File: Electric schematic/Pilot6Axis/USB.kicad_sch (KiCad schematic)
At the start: 20 parts, among them J2 USB_C_Receptacle_USB2.0_16P, Q1 S9014, Q3 S9014, U2 USBLC6-2SC6, U3 CP2102N-Axx-xQFN28

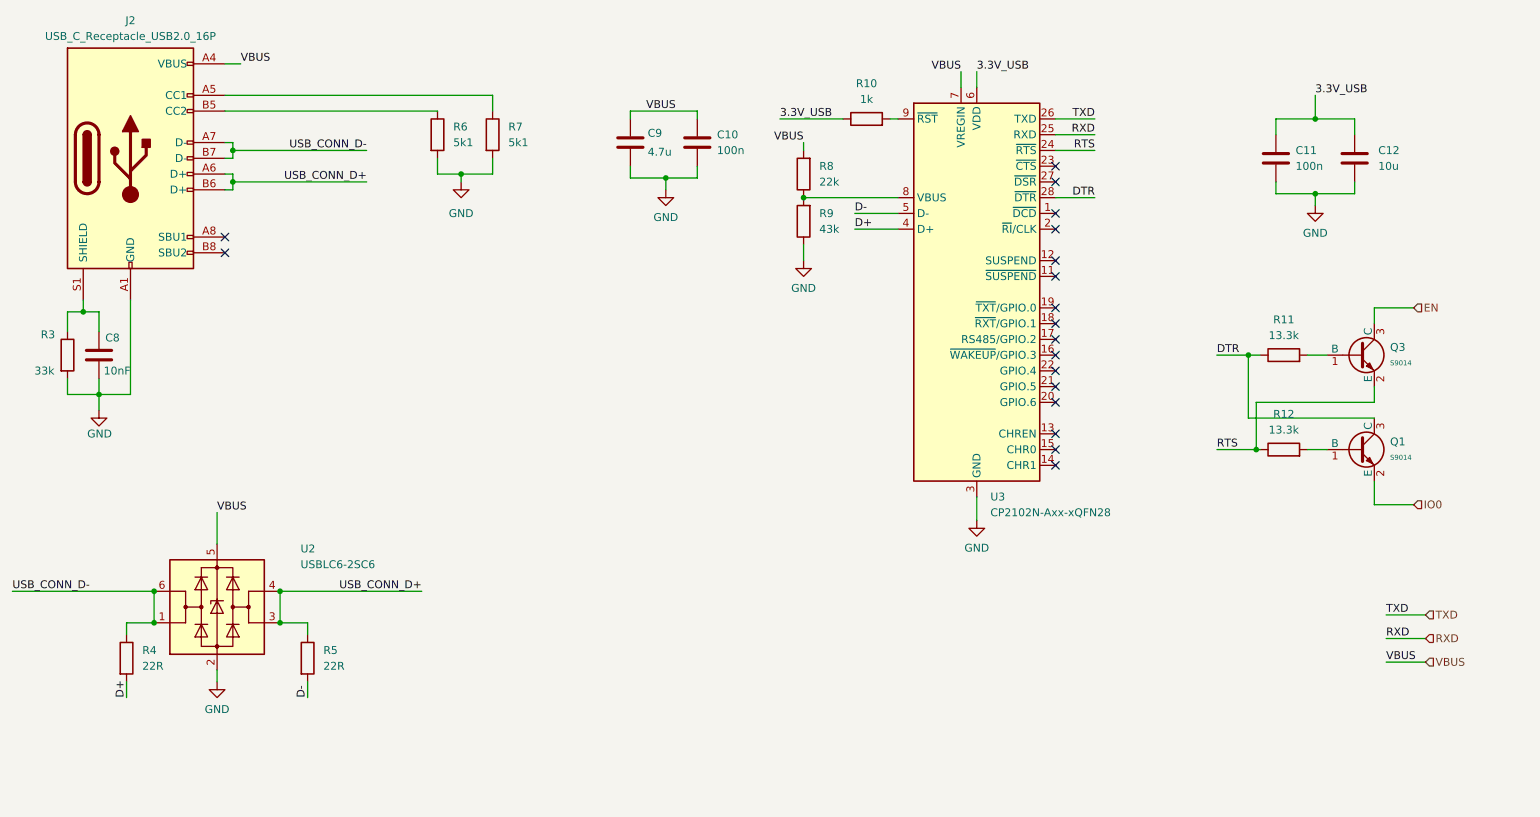
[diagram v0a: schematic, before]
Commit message: update schematic to kicajd 9.0,    fixed usb D=/D- wrongly inerconnected , otherwise pcb seems to be woekring
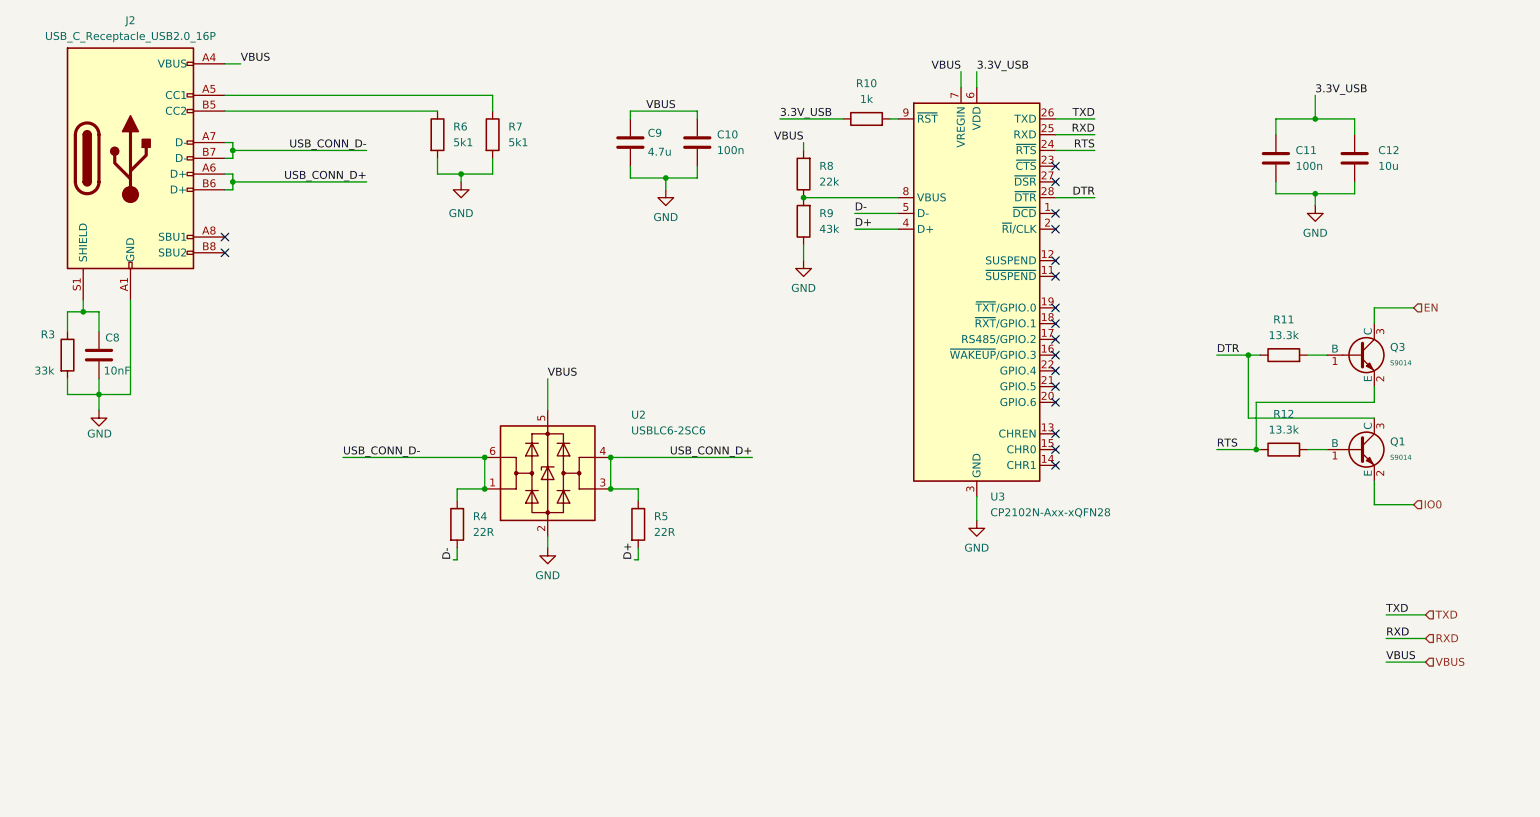
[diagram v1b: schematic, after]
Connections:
- net D+: now also R5.2; no longer R4.2
- net D-: now also R4.2; no longer R5.2
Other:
- moved on the sheet: R4, R5, U2
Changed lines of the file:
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@@
 (kicad_sch
-	(version 20231120)
+	(version 20250114)
 	(generator "eeschema")
-	(generator_version "8.0")
+	(generator_version "9.0")
 	(paper "A4")
 	(junction
@@
 	)
 	(junction
-		(at 50.8 116.84)
+		(at 104.14 95.25)
 		(diameter 0)
 		(color 0 0 0 0)
@@
 	)
 	(junction
-		(at 50.8 121.92)
+		(at 104.14 100.33)
 		(diameter 0)
 		(color 0 0 0 0)
@@
 	)
 	(junction
-		(at 71.12 116.84)
+		(at 124.46 95.25)
 		(diameter 0)
 		(color 0 0 0 0)
@@
 	)
 	(junction
-		(at 71.12 121.92)
+		(at 124.46 100.33)
 		(diameter 0)
 		(color 0 0 0 0)
@@
 	(wire
 		(pts
-			(xy 71.12 121.92) (xy 75.565 121.92)
+			(xy 124.46 100.33) (xy 128.905 100.33)
 		)
 		(stroke
@@
 	(wire
 		(pts
+			(xy 99.695 111.76) (xy 99.695 109.855)
+		)
+		(stroke
+			(width 0)
+			(type default)
+		)
+	)
+	(wire
+		(pts
 			(xy 85.09 45.72) (xy 63.5 45.72)
 		)
@@
 	(wire
 		(pts
-			(xy 46.355 121.92) (xy 46.355 123.825)
+			(xy 99.695 100.33) (xy 99.695 102.235)
 		)
 		(stroke
@@
 	(wire
 		(pts
-			(xy 71.12 116.84) (xy 93.98 116.84)
+			(xy 124.46 95.25) (xy 147.32 95.25)
 		)
 		(stroke
@@
 	(wire
 		(pts
-			(xy 27.94 116.84) (xy 50.8 116.84)
+			(xy 81.28 95.25) (xy 104.14 95.25)
 		)
 		(stroke
@@
 	(wire
 		(pts
+			(xy 128.27 111.76) (xy 128.905 111.76)
+		)
+		(stroke
+			(width 0)
+			(type default)
+		)
+	)
+	(wire
+		(pts
 			(xy 36.83 82.55) (xy 36.83 85.09)
 		)
@@
 	(wire
 		(pts
-			(xy 60.96 104.14) (xy 60.96 109.22)
+			(xy 114.3 82.55) (xy 114.3 87.63)
 		)
 		(stroke
@@
 	(wire
 		(pts
-			(xy 60.96 129.54) (xy 60.96 131.445)
+			(xy 114.3 107.95) (xy 114.3 109.855)
 		)
 		(stroke
@@
 	(wire
 		(pts
-			(xy 62.23 44.45) (xy 63.5 44.45)
+			(xy 128.905 111.76) (xy 128.905 109.855)
 		)
 		(stroke
@@
 	(wire
 		(pts
-			(xy 236.855 78.74) (xy 240.03 78.74)
+			(xy 62.23 44.45) (xy 63.5 44.45)
 		)
 		(stroke
@@
 	(wire
 		(pts
-			(xy 100.33 49.53) (xy 100.33 50.8)
+			(xy 236.855 78.74) (xy 240.03 78.74)
 		)
 		(stroke
@@
 	(wire
 		(pts
-			(xy 238.125 52.705) (xy 238.125 54.61)
+			(xy 100.33 49.53) (xy 100.33 50.8)
 		)
 		(stroke
@@
 	(wire
 		(pts
-			(xy 228.6 93.98) (xy 229.235 93.98)
+			(xy 238.125 52.705) (xy 238.125 54.61)
 		)
 		(stroke
@@
 	(wire
 		(pts
-			(xy 41.91 71.755) (xy 39.37 71.755)
+			(xy 228.6 93.98) (xy 229.235 93.98)
 		)
 		(stroke
@@
 	(wire
 		(pts
-			(xy 238.125 52.705) (xy 244.475 52.705)
+			(xy 41.91 71.755) (xy 39.37 71.755)
 		)
 		(stroke
@@
 	(wire
 		(pts
-			(xy 50.8 116.84) (xy 50.8 121.92)
+			(xy 238.125 52.705) (xy 244.475 52.705)
 		)
 		(stroke
@@
 	(wire
 		(pts
-			(xy 247.65 102.87) (xy 254 102.87)
+			(xy 104.14 95.25) (xy 104.14 100.33)
 		)
 		(stroke
@@
 	(wire
 		(pts
-			(xy 46.355 131.445) (xy 46.355 133.985)
+			(xy 247.65 102.87) (xy 254 102.87)
 		)
 		(stroke
@@
 	(wire
 		(pts
-			(xy 50.8 121.92) (xy 46.355 121.92)
+			(xy 104.14 100.33) (xy 99.695 100.33)
 		)
 		(stroke
@@
 	(wire
 		(pts
-			(xy 75.565 121.92) (xy 75.565 123.825)
+			(xy 128.905 100.33) (xy 128.905 102.235)
 		)
 		(stroke
@@
 	(wire
 		(pts
-			(xy 71.12 116.84) (xy 71.12 121.92)
+			(xy 124.46 95.25) (xy 124.46 100.33)
 		)
 		(stroke
@@
 	(wire
 		(pts
-			(xy 75.565 131.445) (xy 75.565 133.985)
-		)
-		(stroke
-			(width 0)
-			(type default)
-		)
-	)
-	(wire
-		(pts
 			(xy 127.635 50.165) (xy 133.35 50.165)
 		)
@@
 	(wire
 		(pts
+			(xy 99.06 111.76) (xy 99.695 111.76)
+		)
+		(stroke
+			(width 0)
+			(type default)
+		)
+	)
+	(wire
+		(pts
 			(xy 196.215 40.64) (xy 202.565 40.64)
 		)
@@
 	)
 	(label "VBUS"
-		(at 60.96 104.14 0)
+		(at 114.3 82.55 0)
 		(effects
 			(font
@@
 		)
 	)
-	(label "D+"
-		(at 46.355 133.985 90)
-		(effects
-			(font
-				(size 1.27 1.27)
-			)
-			(justify left bottom)
-		)
-	)
 	(label "VBUS"
 		(at 64.77 31.75 0)
@@
 	)
 	(label "USB_CONN_D+"
-		(at 93.98 116.84 180)
+		(at 147.32 95.25 180)
 		(effects
 			(font
@@
 	)
 	(label "USB_CONN_D-"
-		(at 27.94 116.84 0)
+		(at 81.28 95.25 0)
 		(effects
 			(font
@@
 		)
 	)
+	(label "D-"
+		(at 99.06 111.76 90)
+		(effects
+			(font
+				(size 1.27 1.27)
+			)
+			(justify left bottom)
+		)
+	)
 	(label "TXD"
 		(at 249.555 120.65 0)
@@
 		)
 	)
-	(label "D-"
-		(at 75.565 133.985 90)
+	(label "D+"
+		(at 128.27 111.76 90)
 		(effects
 			(font
@@
 	(symbol
 		(lib_id "power:GND")
-		(at 60.96 131.445 0)
+		(at 114.3 109.855 0)
 		(unit 1)
 		(exclude_from_sim no)
@@
 		(fields_autoplaced yes)
 		(property "Reference" "#PWR010"
-			(at 60.96 137.795 0)
+			(at 114.3 116.205 0)
 			(effects
 				(font
@@
 		)
 		(property "Value" "GND"
-			(at 60.96 135.89 0)
+			(at 114.3 114.3 0)
 			(effects
 				(font
@@
 		)
 		(property "Footprint" ""
-			(at 60.96 131.445 0)
+			(at 114.3 109.855 0)
 			(effects
 				(font
@@
 		)
 		(property "Datasheet" ""
-			(at 60.96 131.445 0)
+			(at 114.3 109.855 0)
 			(effects
 				(font
@@
 		)
 		(property "Description" ""
-			(at 60.96 131.445 0)
+			(at 114.3 109.855 0)
 			(effects
 				(font
@@
 	(symbol
 		(lib_id "Power_Protection:USBLC6-2SC6")
-		(at 60.96 119.38 0)
+		(at 114.3 97.79 0)
 		(unit 1)
 		(exclude_from_sim no)
@@
 		(dnp no)
 		(property "Reference" "U2"
-			(at 74.422 109.982 0)
+			(at 127.762 88.392 0)
 			(effects
 				(font
@@
 		)
 		(property "Value" "USBLC6-2SC6"
-			(at 74.422 112.522 0)
+			(at 127.762 90.932 0)
 			(effects
 				(font
@@
 		)
 		(property "Footprint" "Package_TO_SOT_SMD:SOT-23-6"
-			(at 60.96 132.08 0)
+			(at 114.3 110.49 0)
 			(effects
 				(font
@@
 		)
 		(property "Datasheet" "https://www.st.com/resource/en/datasheet/usblc6-2.pdf"
-			(at 66.04 110.49 0)
+			(at 119.38 88.9 0)
 			(effects
 				(font
@@
 		)
 		(property "Description" ""
-			(at 60.96 119.38 0)
+			(at 114.3 97.79 0)
 			(effects
 				(font
@@
 		)
 		(property "LCSC" "C5180249"
-			(at 62.6111 106.68 0)
+			(at 115.9511 85.09 0)
 			(effects
 				(font
@@
 	(symbol
 		(lib_id "Device:R")
-		(at 46.355 127.635 0)
+		(at 99.695 106.045 0)
 		(unit 1)
 		(exclude_from_sim no)
@@
 		(fields_autoplaced yes)
 		(property "Reference" "R4"
-			(at 48.895 126.365 0)
+			(at 102.235 104.775 0)
 			(effects
 				(font
@@
 		)
 		(property "Value" "22R"
-			(at 48.895 128.905 0)
+			(at 102.235 107.315 0)
 			(effects
 				(font
@@
 		)
 		(property "Footprint" "Resistor_SMD:R_0603_1608Metric"
-			(at 44.577 127.635 90)
+			(at 97.917 106.045 90)
 			(effects
 				(font
@@
 		)
 		(property "Datasheet" "~"
-			(at 46.355 127.635 0)
+			(at 99.695 106.045 0)
 			(effects
 				(font
@@
 		)
 		(property "Description" ""
-			(at 46.355 127.635 0)
+			(at 99.695 106.045 0)
 			(effects
 				(font
@@
 		)
 		(property "LCSC" "C71618"
-			(at 48.895 126.365 0)
+			(at 102.235 104.775 0)
 			(effects
 				(font
@@
 	(symbol
 		(lib_id "Device:R")
-		(at 75.565 127.635 0)
+		(at 128.905 106.045 0)
 		(unit 1)
 		(exclude_from_sim no)
@@
 		(fields_autoplaced yes)
 		(property "Reference" "R5"
-			(at 78.105 126.365 0)
+			(at 131.445 104.775 0)
 			(effects
 				(font
@@
 		)
 		(property "Value" "22R"
-			(at 78.105 128.905 0)
+			(at 131.445 107.315 0)
 			(effects
 				(font
@@
 		)
 		(property "Footprint" "Resistor_SMD:R_0603_1608Metric"
-			(at 73.787 127.635 90)
+			(at 127.127 106.045 90)
 			(effects
 				(font
@@
 		)
 		(property "Datasheet" "~"
-			(at 75.565 127.635 0)
+			(at 128.905 106.045 0)
 			(effects
 				(font
@@
 		)
 		(property "Description" ""
-			(at 75.565 127.635 0)
+			(at 128.905 106.045 0)
 			(effects
 				(font
@@
 		)
 		(property "LCSC" "C71618"
-			(at 78.105 126.365 0)
+			(at 131.445 104.775 0)
 			(effects
 				(font

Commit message: upgrade board to use USB BD for power delivery and addded SPI screen conector
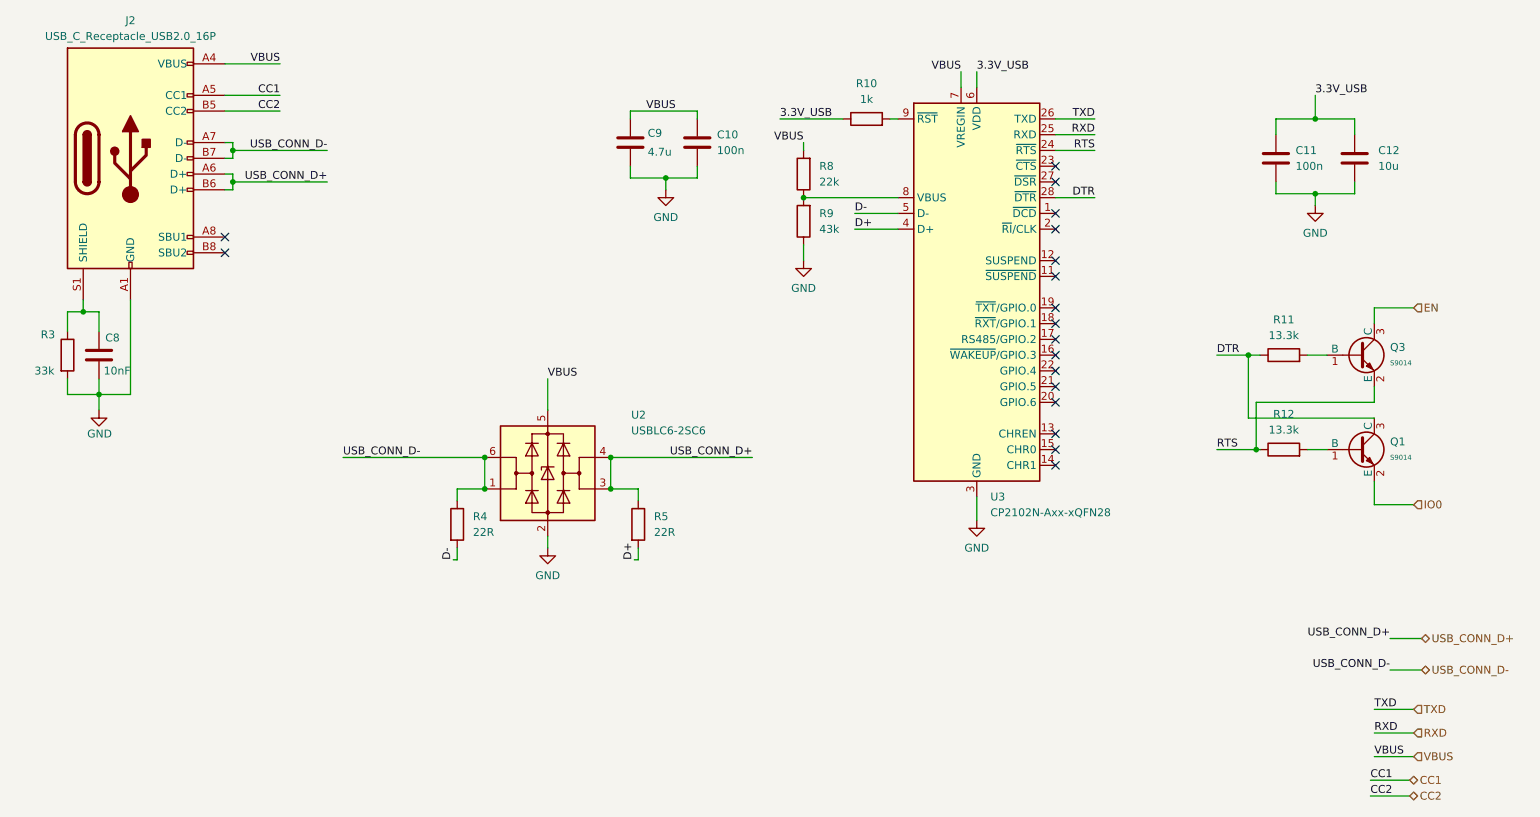
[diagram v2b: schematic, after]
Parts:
- removed R6, R7: 5k1, Resistor_SMD:R_0603_1608Metric, symbol Device:R
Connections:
- net CC1: now reaches J2.A5 (CC1)
- net CC2: now reaches J2.B5 (CC2)
